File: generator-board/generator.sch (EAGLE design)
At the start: 41 parts, among them IC1 MAX1771, Q1 IRF740DPACK

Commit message: adding testpad, starting counting board
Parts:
- added H1, H2, H3, H4: MOUNT-HOLE3.0, Mounting:MOUNT-HOLE3.0
- added TP1, TP2, TP3, TP4: TP, Testpoint:TP
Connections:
- net GND: now also TP4.P$1
- net N$14: now also TP3.P$1
- net N$16: now also TP2.P$1
- net N$26: now also TP1.P$1
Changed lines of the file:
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@@
 <?xml version="1.0" encoding="utf-8"?>
 <!DOCTYPE eagle SYSTEM "eagle.dtd">
-<eagle version="6.5.0">
+<eagle version="6.6.0">
 <drawing>
 <settings>
@@
 <part name="D13" library="diode" deviceset="1N4148" device="DO35-7"/>
 <part name="R9" library="rcl" deviceset="R-TRIMM" device="3103"/>
+<part name="TP1" library="Testpoint" deviceset="TP" device=""/>
+<part name="TP2" library="Testpoint" deviceset="TP" device=""/>
+<part name="TP3" library="Testpoint" deviceset="TP" device=""/>
+<part name="H1" library="Mounting" deviceset="MOUNT-HOLE" device="3.0"/>
+<part name="H2" library="Mounting" deviceset="MOUNT-HOLE" device="3.0"/>
+<part name="H3" library="Mounting" deviceset="MOUNT-HOLE" device="3.0"/>
+<part name="H4" library="Mounting" deviceset="MOUNT-HOLE" device="3.0"/>
+<part name="TP4" library="Testpoint" deviceset="TP" device=""/>
+<part name="GND11" library="supply1" deviceset="GND" device=""/>
 </parts>
 <sheets>
@@
 <instance part="D13" gate="G$1" x="195.58" y="63.5" rot="R270"/>
 <instance part="R9" gate="G$1" x="58.42" y="20.32"/>
+<instance part="TP1" gate="G$1" x="195.58" y="43.18" rot="R180"/>
+<instance part="TP2" gate="G$1" x="180.34" y="43.18" rot="R180"/>
+<instance part="TP3" gate="G$1" x="165.1" y="43.18" rot="R180"/>
+<instance part="H1" gate="G$1" x="182.88" y="25.4"/>
+<instance part="H2" gate="G$1" x="187.96" y="25.4"/>
+<instance part="H3" gate="G$1" x="187.96" y="20.32"/>
+<instance part="H4" gate="G$1" x="185.42" y="20.32"/>
+<instance part="TP4" gate="G$1" x="152.4" y="43.18" rot="R180"/>
+<instance part="GND11" gate="1" x="152.4" y="45.72" rot="R180"/>
 </instances>
 <busses>
@@
 <pinref part="GND9" gate="1" pin="GND"/>
 <pinref part="R9" gate="G$1" pin="A"/>
+</segment>
+<segment>
+<pinref part="TP4" gate="G$1" pin="P$1"/>
+<pinref part="GND11" gate="1" pin="GND"/>
 </segment>
 </net>
@@
 <pinref part="C9" gate="G$1" pin="1"/>
 <junction x="172.72" y="53.34"/>
+<pinref part="TP3" gate="G$1" pin="P$1"/>
+<wire x1="165.1" y1="43.18" x2="165.1" y2="53.34" width="0.1524" layer="91"/>
 </segment>
 </net>
@@
 <pinref part="C16" gate="G$1" pin="1"/>
 <junction x="187.96" y="53.34"/>
+<pinref part="TP2" gate="G$1" pin="P$1"/>
+<wire x1="180.34" y1="43.18" x2="180.34" y2="53.34" width="0.1524" layer="91"/>
 </segment>
 </net>
@@
 <wire x1="195.58" y1="53.34" x2="195.58" y2="43.18" width="0.1524" layer="91"/>
 <junction x="195.58" y="53.34"/>
-</segment>
-</net>
+<pinref part="TP1" gate="G$1" pin="P$1"/>
+</segment>
+</net>

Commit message: done gen bom, almost done coutner
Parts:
- removed H1, H2, H3, H4: MOUNT-HOLE3.0, Mounting:MOUNT-HOLE3.0
- added JP1: (no value), SparkFun-Connectors:M03PTH
- C1: value (none) -> 100n
- C10, C11, C12, C13, C14, C15, C16, C4, C5, C6, C7, C8, C9: FARNELL (none) -> 1855877
- C2: value (none) -> 47u; FARNELL (none) -> 9452460; VOLTAGE (none) -> 16V
- C3: value (none) -> 2.2u
- D1, D10, D11, D12, D13, D2, D3, D4, D5, D6, D7, D8, D9: FARNELL (none) -> 1625213
- L1: FARNELL (none) -> 2061654
- Q1: FARNELL (none) -> 2453433
- R1: value (none) -> 0.2; FARNELL (none) -> 2328089
- R2, R3, R4, R5: value (none) -> 6.8M; FARNELL (none) -> 2138708
- R6: value (none) -> 560k
- R8: value (none) -> 100k
- R9: value (none) -> 47k
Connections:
- removed net N$22: IC1.FB, R5.P$1, R6.P$2
- new net N$17: IC1.FB, R5.P$1, R9.E, R9.S
- net GND: now also JP1.1, R6.P$2; no longer R9.A
- net N$23: now also R9.A; no longer R9.E, R9.S
- net N$24: now also JP1.2
- net N$4: now also JP1.3
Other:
- moved on the sheet: R6, R9

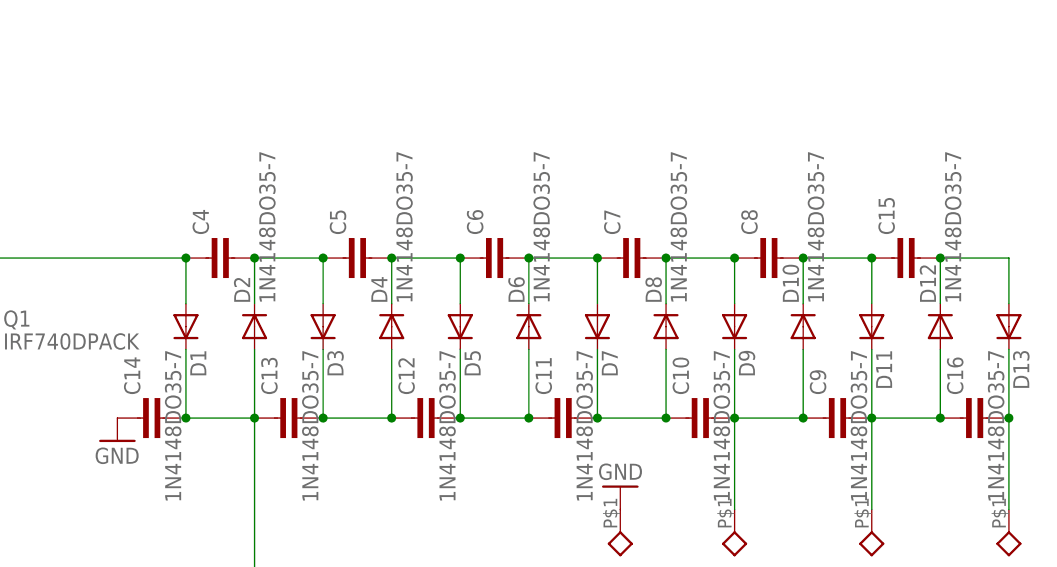
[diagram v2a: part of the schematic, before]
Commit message: adding part ordering numbers
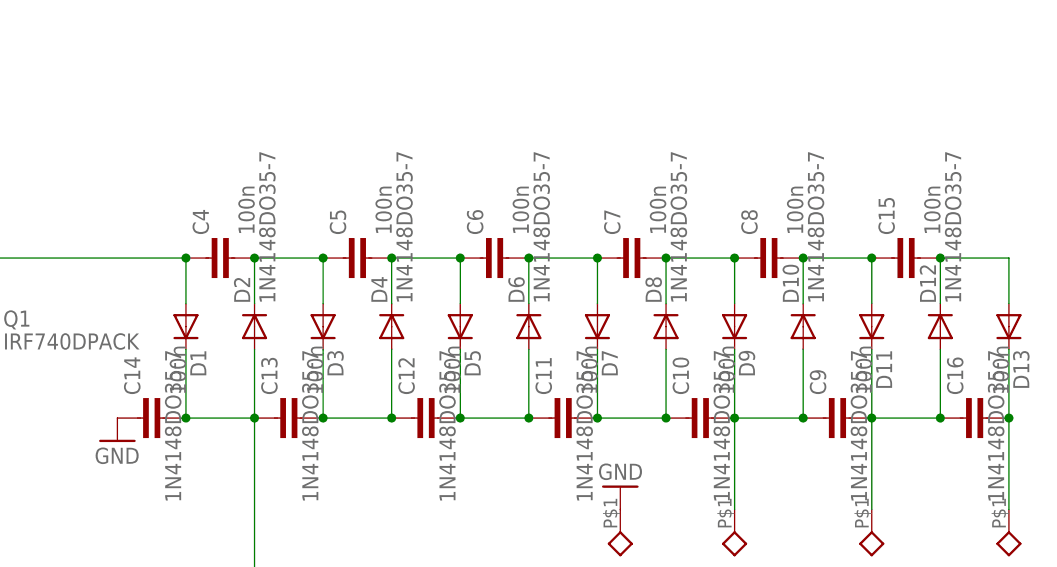
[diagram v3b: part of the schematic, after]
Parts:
- C1: FARNELL (none) -> 2495332
- C10, C11, C12, C13, C14, C15, C16, C4, C5, C6, C7, C8, C9: value (none) -> 100n
- C3: FARNELL (none) -> 2496923
- R9: FARNELL (none) -> 1771727

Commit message: almost done
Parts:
- removed JP1: (no value), SparkFun-Connectors:M03PTH
- removed R9: 47k, rcl:R-TRIMM3103
- removed TP1, TP2, TP3, TP4: TP, Testpoint:TP
- added J2: HV_GEN-HOLE, generator-lib:HV_GEN-HOLE
- added R7: 6.8M, passives-7351:RESISTOR0603-N
- C1: device passives-7351:CAPACITOR0603-N -> passives-7351:CAPACITOR1206-N; FARNELL 2495332 -> 1855877
- C15: device passives-7351:CAPACITOR1206-N -> passives-7351:CAPACITOR0603-N; FARNELL 1855877 -> 2495332
- C16: value 100n -> 2.2u; device passives-7351:CAPACITOR1206-N -> passives-7351:CAPACITOR0603-N; FARNELL 1855877 -> 2496923
- C2: value 47u -> 100n; device rcl:CPOL-EUE2-5 -> passives-7351:CAPACITOR1206-N; FARNELL 9452460 -> 1855877; VOLTAGE 16V -> (none)
- C3: value 2.2u -> 100n; device passives-7351:CAPACITOR0603-N -> passives-7351:CAPACITOR1206-N; FARNELL 2496923 -> 1855877
- C7: value 100n -> 47u; device passives-7351:CAPACITOR1206-N -> rcl:CPOL-EUE2-5; FARNELL 1855877 -> 9452460; VOLTAGE (none) -> 16V
- R2: value 6.8M -> 100k; FARNELL 2138708 -> (none)
- R3: value 6.8M -> 560k; FARNELL 2138708 -> (none)
- R4: value 6.8M -> 47k; device passives-7351:RESISTOR0603-N -> rcl:R-TRIMM3103; FARNELL 2138708 -> 1771727
- R6: value 560k -> 6.8M; FARNELL (none) -> 2138708
- R8: value 100k -> 6.8M; FARNELL (none) -> 2138708
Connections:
- removed net N$24: IC1.SHDN, JP1.2, R8.P$2
- removed net N$4: C2.+, C3.1, IC1.V+, J1.+, JP1.3, L1.2
- new net SHDN: IC1.SHDN, J2.SHDN, R2.P$2
- new net VIN: C16.1, C7.+, IC1.V+, J1.+, J2.VIN, L1.2
- net GND: now also C15.2, C16.2, C7.-, C8.1, J2.GND, J2.HV_GND, R2.P$1, R3.P$2; no longer C1.2, C14.1, C2.-, C3.2, JP1.1, R6.P$2, R8.P$1, TP4.P$1
- net N$10: now also C10.2; no longer C12.2
- net N$11: now also C3.2, C4.1; no longer C6.2, C7.1
- net N$12: now also C12.1; no longer C10.1
- net N$13: now also C4.2, C5.1; no longer C7.2, C8.1
- net N$14: now also C12.2, C13.1, J2.HV1; no longer C10.2, C9.1, TP3.P$1
- net N$15: now also C5.2, C6.1; no longer C15.1, C8.2
- net N$16: now also C13.2, C14.1, J2.HV2; no longer C16.1, C9.2, TP2.P$1
- net N$17: now also R4.E, R4.S, R6.P$1; no longer R5.P$1, R9.E, R9.S
- net N$18: now also R5.P$1, R8.P$2; no longer R2.P$1, R3.P$2
- net N$19: now also R7.P$2, R8.P$1; no longer R3.P$1, R4.P$2
- net N$20: now also R6.P$2, R7.P$1; no longer R4.P$1, R5.P$2
- net N$23: now also R3.P$1, R4.A; no longer R6.P$1, R9.A
- net N$25: now also C6.2; no longer C15.2
- net N$26: now also C14.2, J2.HV3; no longer C16.2, TP1.P$1
- net N$3: now also C8.2, C9.1, R5.P$2; no longer C13.1, C14.2, R2.P$2
- net N$5: now also C15.1; no longer C1.1
- net N$6: now also C1.1; no longer C4.1
- net N$7: now also C1.2, C2.1; no longer C4.2, C5.1
- net N$8: now also C10.1, C9.2; no longer C12.1, C13.2
- net N$9: now also C2.2, C3.1; no longer C5.2, C6.1
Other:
- moved on the sheet: C1, C10, C12, C13, C14, C15, C16, C3, C4, C5, C6, C8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

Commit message: about to panelize
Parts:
- added SV1: (no value), con-lstb:MA06-1
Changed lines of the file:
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@@
 <?xml version="1.0" encoding="utf-8"?>
 <!DOCTYPE eagle SYSTEM "eagle.dtd">
-<eagle version="6.5.0">
+<eagle version="6.6.0">
 <drawing>
 <settings>
@@
 <part name="GND13" library="supply1" deviceset="GND" device=""/>
 <part name="GND14" library="supply1" deviceset="GND" device=""/>
+<part name="SV1" library="con-lstb" deviceset="MA06-1" device=""/>
 </parts>
 <sheets>
@@
 <instance part="GND13" gate="1" x="167.64" y="12.7"/>
 <instance part="GND14" gate="1" x="137.16" y="17.78"/>
+<instance part="SV1" gate="1" x="12.7" y="10.16"/>
 </instances>
 <busses>

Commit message: final board, started firmware
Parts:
- removed SV1: (no value), con-lstb:MA06-1
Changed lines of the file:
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@@
 <part name="GND13" library="supply1" deviceset="GND" device=""/>
 <part name="GND14" library="supply1" deviceset="GND" device=""/>
-<part name="SV1" library="con-lstb" deviceset="MA06-1" device=""/>
 </parts>
 <sheets>
@@
 <instance part="GND13" gate="1" x="167.64" y="12.7"/>
 <instance part="GND14" gate="1" x="137.16" y="17.78"/>
-<instance part="SV1" gate="1" x="12.7" y="10.16"/>
 </instances>
 <busses>
